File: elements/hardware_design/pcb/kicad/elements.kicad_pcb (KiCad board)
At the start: 2 copper layers, 164.5 x 106 mm, 198 parts, among them IC1 LM4040B10, IC10 STM32F405RGT6, IC11 4051PW, IC12 WM8731, IC13 MCP6004, IC14 LME49720, IC2 LM1117-3.3, IC3 4051PW, IC4 LM1117-3.3, IC5 4051PW, IC6 MCP6004, IC7 MCP6004, IC8 4051PW, IC9 MCP6002, J1 PJ301_THONKICONN6, J10 PJ301_THONKICONN6, J11 PJ301_THONKICONN6, J12 PJ301_THONKICONN6, J13 PJ301_THONKICONN6, J14 PJ301_THONKICONN6, J15 PJ301_THONKICONN6, J16 PJ301_THONKICONN6, J17 PJ301_THONKICONN6, J18 PJ301_THONKICONN6, J2 PJ301_THONKICONN6, J3 PJ301_THONKICONN6, J4 PJ301_THONKICONN6, J5 PJ301_THONKICONN6, J6 PJ301_THONKICONN6, J7 PJ301_THONKICONN6, J8 PJ301_THONKICONN6, J9 PJ301_THONKICONN6, Q1 8MHz, Q2 MMBT3904, SW1 LP4OA1PBCT

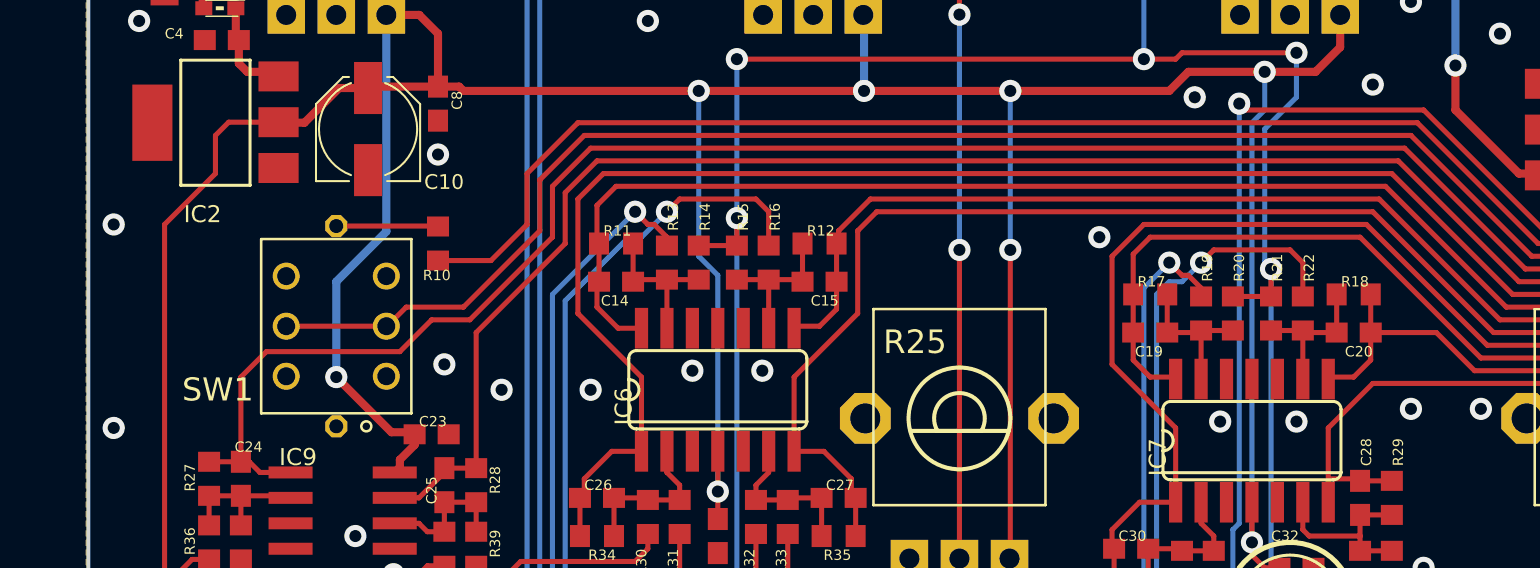
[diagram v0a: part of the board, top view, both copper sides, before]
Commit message: changed led/switch
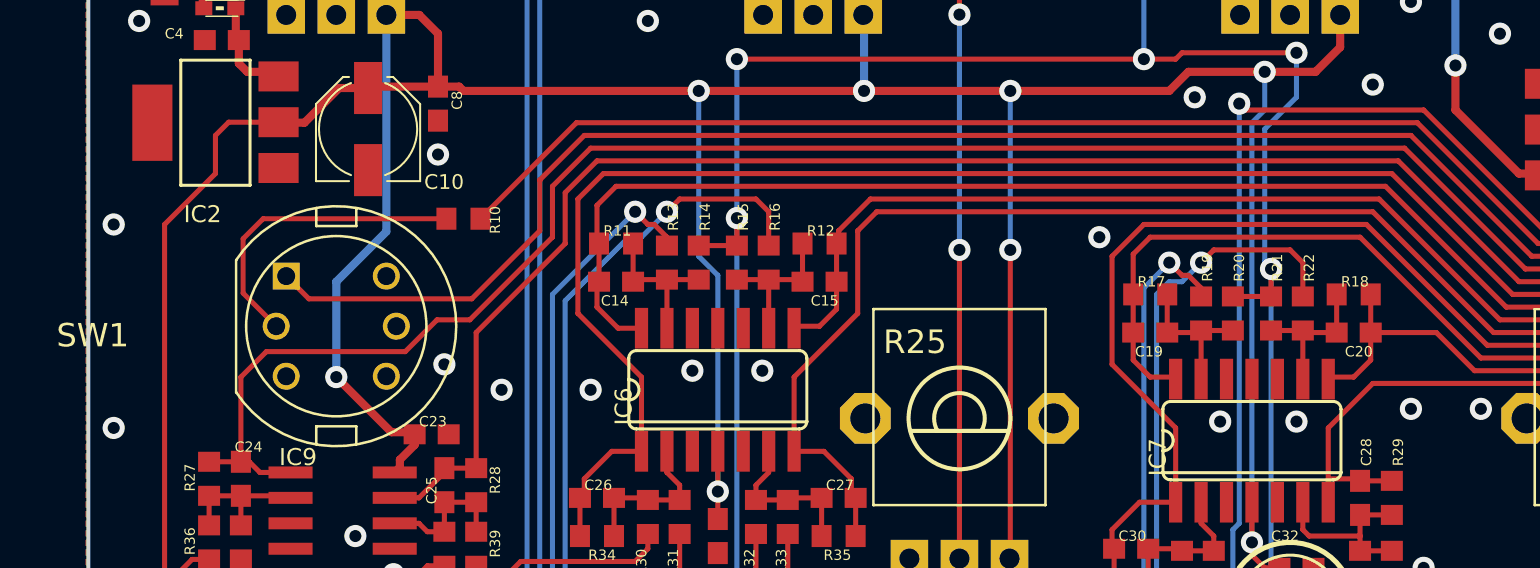
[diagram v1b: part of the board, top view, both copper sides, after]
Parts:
- removed U$2: , elements:ROHS_BIG
- JP2: value (none) -> M06SIP
- L1, L2: value (none) -> WE-CBF_0603
- SW1: value LP4OA1PBCT -> SW_MEC_5G_2LED; footprint elements:LP4OA1PBCT -> Supercell 1.3:C&K_D6R
- SW2, SW3: value (none) -> EVQQ2
- moved R10 1.77 mm to (85.0, 79.0), turned to 180 degrees
- turned SW1 to 0 degrees
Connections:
- net BOOT_FLASH renamed /elements_2/BOOT_FLASH
- net I2C_SCL renamed /elements_2/I2C_SCL
- net I2C_SDA renamed /elements_2/I2C_SDA
- net I2S_LRCK renamed /elements_2/I2S_LRCK
- net I2S_MCK renamed /elements_2/I2S_MCK
- net I2S_SCK renamed /elements_2/I2S_SCK
- net I2S_SIN renamed /elements_2/I2S_SIN
- net I2S_SOUT renamed /elements_2/I2S_SOUT
- net JTCK renamed /elements_2/JTCK
- net JTDI renamed /elements_2/JTDI
- net JTDO renamed /elements_2/JTDO
- net JTMS renamed /elements_2/JTMS
- net LOUT_JACK renamed Net-(J8-PadP3)
- net RESET renamed /elements_2/RESET
- net ROUT_JACK renamed Net-(J7-PadP3)
- net RX renamed /elements_2/RX
- net TX renamed /elements_2/TX
- IC10 pad 39: (no net) -> unconnected-(IC10-Pad39)
- IC10 pad 40: (no net) -> unconnected-(IC10-Pad40)
- IC10 pad 45: (no net) -> unconnected-(IC10-Pad45)
- IC10 pad 51: (no net) -> unconnected-(IC10-Pad51)
- IC10 pad 52: (no net) -> unconnected-(IC10-Pad52)
- IC10 pad 53: (no net) -> unconnected-(IC10-Pad53)
- IC10 pad 54: (no net) -> unconnected-(IC10-Pad54)
- IC10 pad 56: (no net) -> unconnected-(IC10-Pad56)
- IC10 pad 62: (no net) -> unconnected-(IC10-Pad62)
- IC12 pad 10: (no net) -> unconnected-(IC12-Pad10)
- IC12 pad 17: (no net) -> unconnected-(IC12-Pad17)
- IC12 pad 18: (no net) -> unconnected-(IC12-Pad18)
- IC12 pad 2: (no net) -> unconnected-(IC12-Pad2)
- IC12 pad 26: (no net) -> unconnected-(IC12-Pad26)
- IC12 pad 9: (no net) -> unconnected-(IC12-Pad9)
- J1 pad P2: (no net) -> unconnected-(J1-PadP2)
- J10 pad P2: (no net) -> unconnected-(J10-PadP2)
- J11 pad P2: (no net) -> unconnected-(J11-PadP2)
- J12 pad P2: (no net) -> unconnected-(J12-PadP2)
- J13 pad P2: (no net) -> unconnected-(J13-PadP2)
- J14 pad P2: (no net) -> unconnected-(J14-PadP2)
- J15 pad P2: (no net) -> unconnected-(J15-PadP2)
- J16 pad P2: (no net) -> unconnected-(J16-PadP2)
- J17 pad P2: (no net) -> unconnected-(J17-PadP2)
- J18 pad P2: (no net) -> unconnected-(J18-PadP2)
- J2 pad P2: (no net) -> unconnected-(J2-PadP2)
- J4 pad P2: (no net) -> unconnected-(J4-PadP2)
- J5 pad P2: (no net) -> unconnected-(J5-PadP2)
- J6 pad P2: (no net) -> unconnected-(J6-PadP2)
- J7 pad P2: (no net) -> unconnected-(J7-PadP2)
- J8 pad P2: (no net) -> unconnected-(J8-PadP2)
- J9 pad P2: (no net) -> unconnected-(J9-PadP2)
- JP1 pad 7: (no net) -> unconnected-(JP1-Pad7)
- JP2 pad 2: (no net) -> unconnected-(JP2-Pad2)
- JP2 pad 3: (no net) -> unconnected-(JP2-Pad3)
- JP2 pad 6: (no net) -> unconnected-(JP2-Pad6)
- R10 pad 2: N$38 -> Net-(R10-Pad2)
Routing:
- net Net-(R10-Pad2): track 0.00 -> 15.6 mm
- net N$38: track 5.09 -> 0.00 mm
- net LED_GATE: track 107.7 -> 103.3 mm

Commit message: change LME49720 to tl072
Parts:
- IC14: value LME49720 -> TL072
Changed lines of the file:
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@@
       (effects (font (size 0.84836 0.84836) (thickness 0.16764)) (justify left))
     )
-    (fp_text value "LME49720" (at -2.2225 1.0795) (layer "F.Fab")
+    (fp_text value "TL072" (at -2.2225 1.0795) (layer "F.Fab")
       (effects (font (size 0.44196 0.44196) (thickness 0.16764)) (justify left))
     )

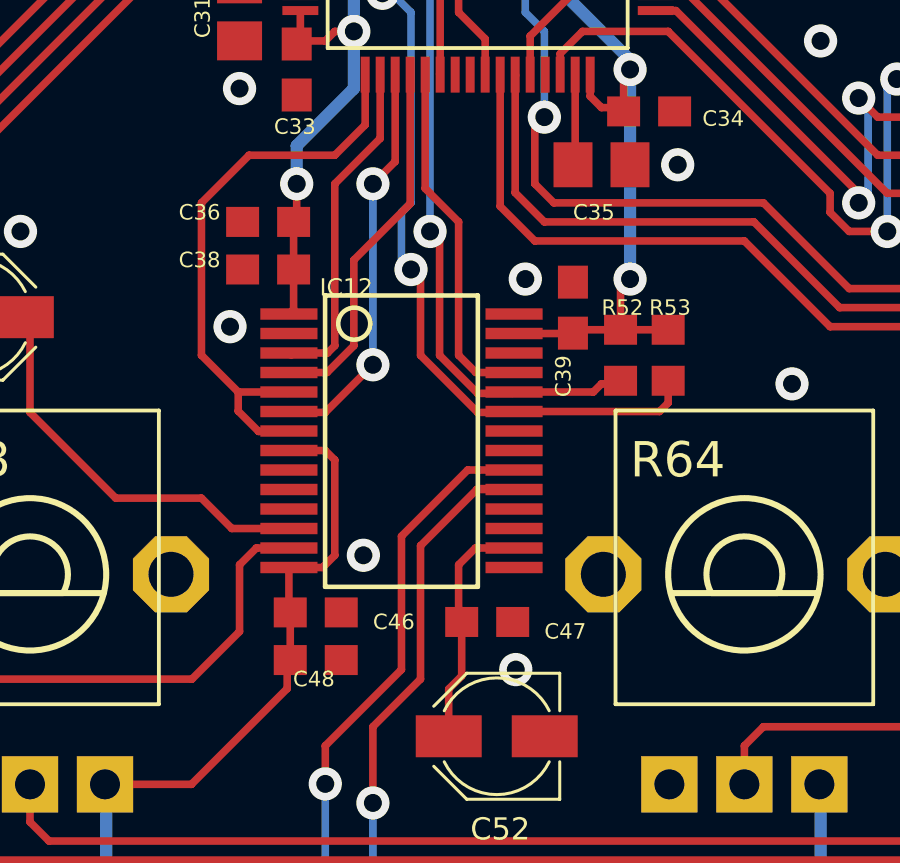
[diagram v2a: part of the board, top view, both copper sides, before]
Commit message: swap wm8731 package (haven't drawn traces yet)
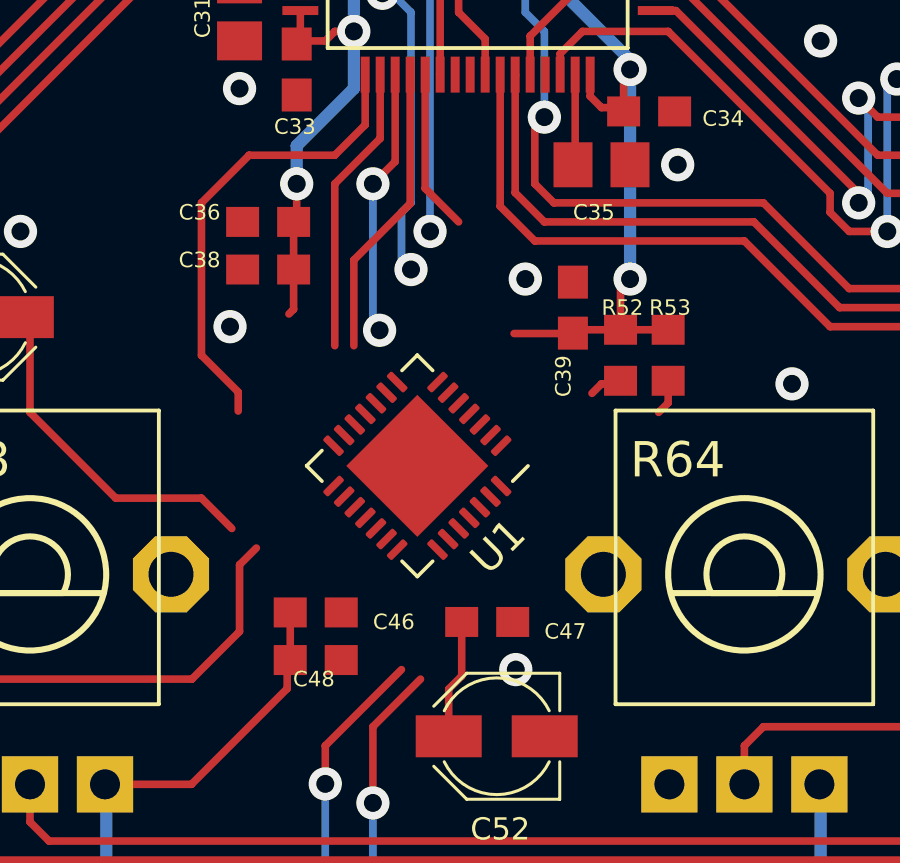
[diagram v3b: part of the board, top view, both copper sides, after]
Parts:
- removed IC12: WM8731, elements:SSOP28
- added U1: WM8731CLSEFL, Package_DFN_QFN:QFN-28-1EP_5x5mm_P0.5mm_EP3.35x3.35mm, F.Cu at (163.0, 112.5)
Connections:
- R52 pad 1: /elements_2/I2C_SCL -> /elements_2/I2C_SDA
- R53 pad 1: /elements_2/I2C_SDA -> /elements_2/I2C_SCL
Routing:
- net /elements_2/I2C_SDA: track 25.9 -> 14.5 mm
- net RIN: track 94.1 -> 84.5 mm
- net /elements_2/I2C_SCL: track 24.1 -> 14.8 mm
- net LIN: track 94.1 -> 85.0 mm
- net +3V3_A: track 885.1 -> 877.1 mm
- net /elements_2/I2S_MCK: track 11.9 -> 5.37 mm
- net /elements_2/I2S_SIN: track 13.4 -> 8.92 mm
- net Net-(U1-Pad20): track 8.02 -> 4.13 mm
- net /elements_2/I2S_LRCK: track 19.4 -> 15.7 mm
- net /elements_2/I2S_SOUT: track 12.3 -> 9.81 mm
- net LOUT: track 13.5 -> 11.6 mm
- net /elements_2/I2S_SCK: track 11.4 -> 9.66 mm
- net ROUT: track 20.1 -> 19.1 mm
- net GND: vias 146 -> 145

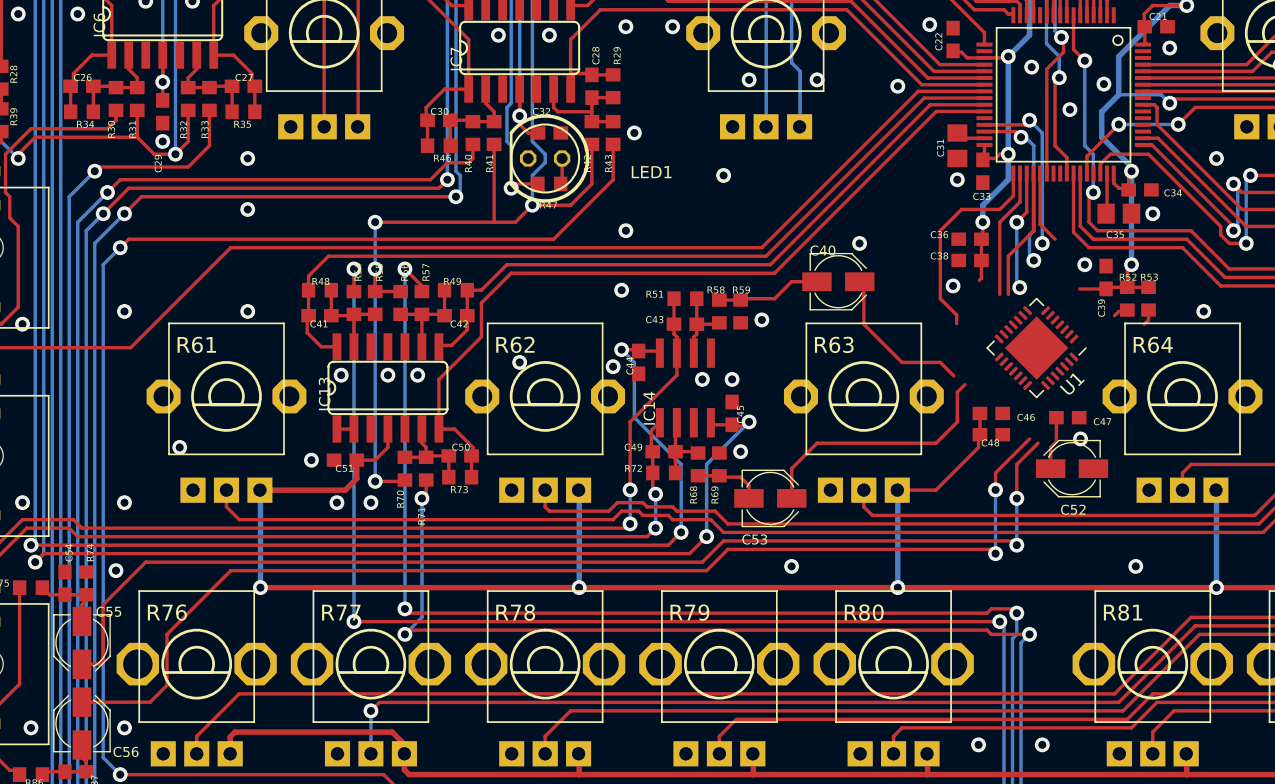
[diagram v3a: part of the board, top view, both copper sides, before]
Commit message: traces drawn for wm8731
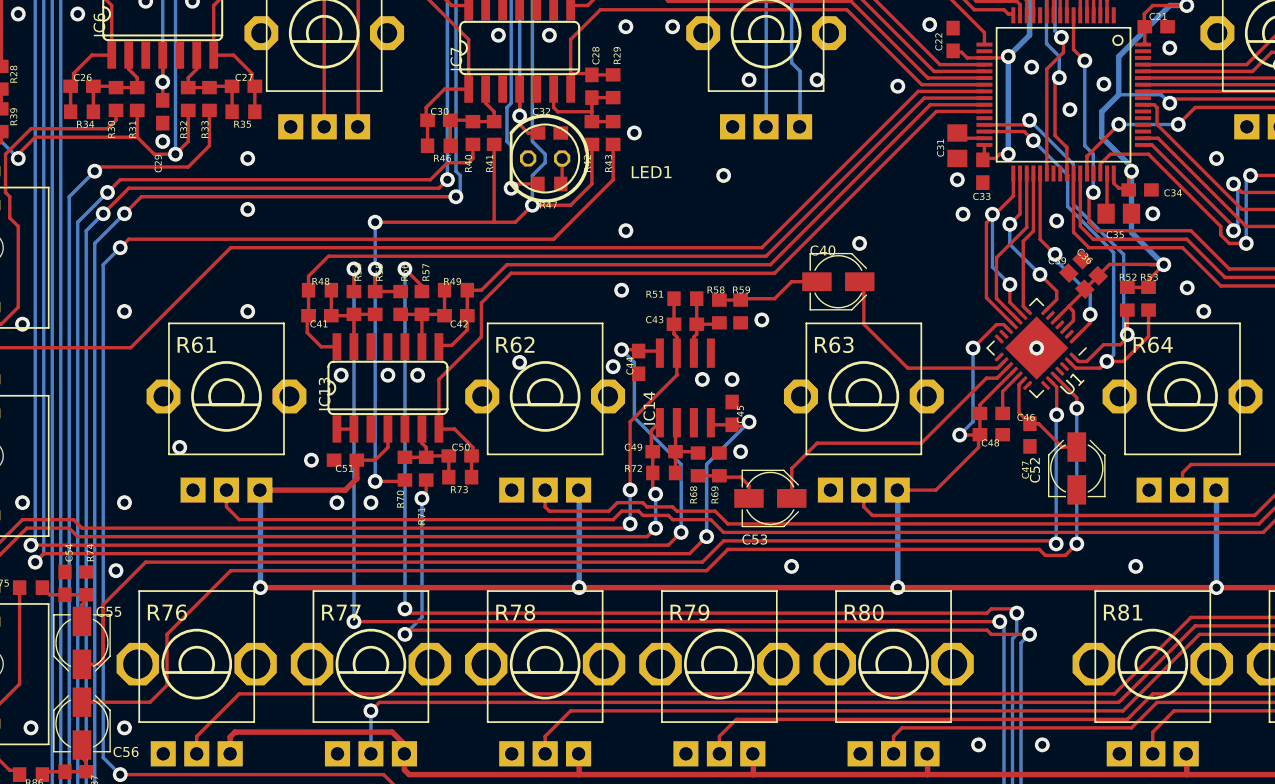
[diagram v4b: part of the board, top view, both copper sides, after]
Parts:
- removed C38: 100n, elements:C0603
- moved C36 9.22 mm to (167.0, 106.5), turned to 135 degrees
- moved C47 3.11 mm to (162.5, 119.0), turned to -90 degrees
- moved C39 2.20 mm to (166.0, 107.5), turned to 135 degrees
- moved C52 0.35 mm to (166.0, 121.5), turned to 90 degrees
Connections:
- R52 pad 1: /elements_2/I2C_SDA -> /elements_2/I2C_SCL
- R53 pad 1: /elements_2/I2C_SCL -> /elements_2/I2C_SDA
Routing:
- net /elements_2/I2C_SDA: track 14.5 -> 32.2 mm
- net +3V3_A: track 877.1 -> 893.3 mm, vias 25 -> 27
- net /elements_2/I2C_SCL: track 14.8 -> 29.5 mm
- net LIN: track 85.0 -> 95.1 mm
- net /elements_2/I2S_MCK: track 5.37 -> 14.4 mm, vias 0 -> 2
- net RIN: track 84.5 -> 91.5 mm
- net /elements_2/I2S_LRCK: track 15.7 -> 21.5 mm, vias 0 -> 2
- net Net-(C47-Pad1): track 4.13 -> 7.90 mm
- net LOUT: track 11.6 -> 15.3 mm
- net /elements_2/I2S_SIN: track 8.92 -> 12.6 mm, vias 2 -> 0
- net GND: track 0.04 -> 3.32 mm, vias 145 -> 146
- net /elements_2/I2S_SCK: track 9.66 -> 12.4 mm, vias 0 -> 2
- net ROUT: track 19.1 -> 21.6 mm
- net /elements_2/I2S_SOUT: track 9.81 -> 10.7 mm
- net +3V3: track 217.5 -> 218.0 mm, vias 12 -> 11

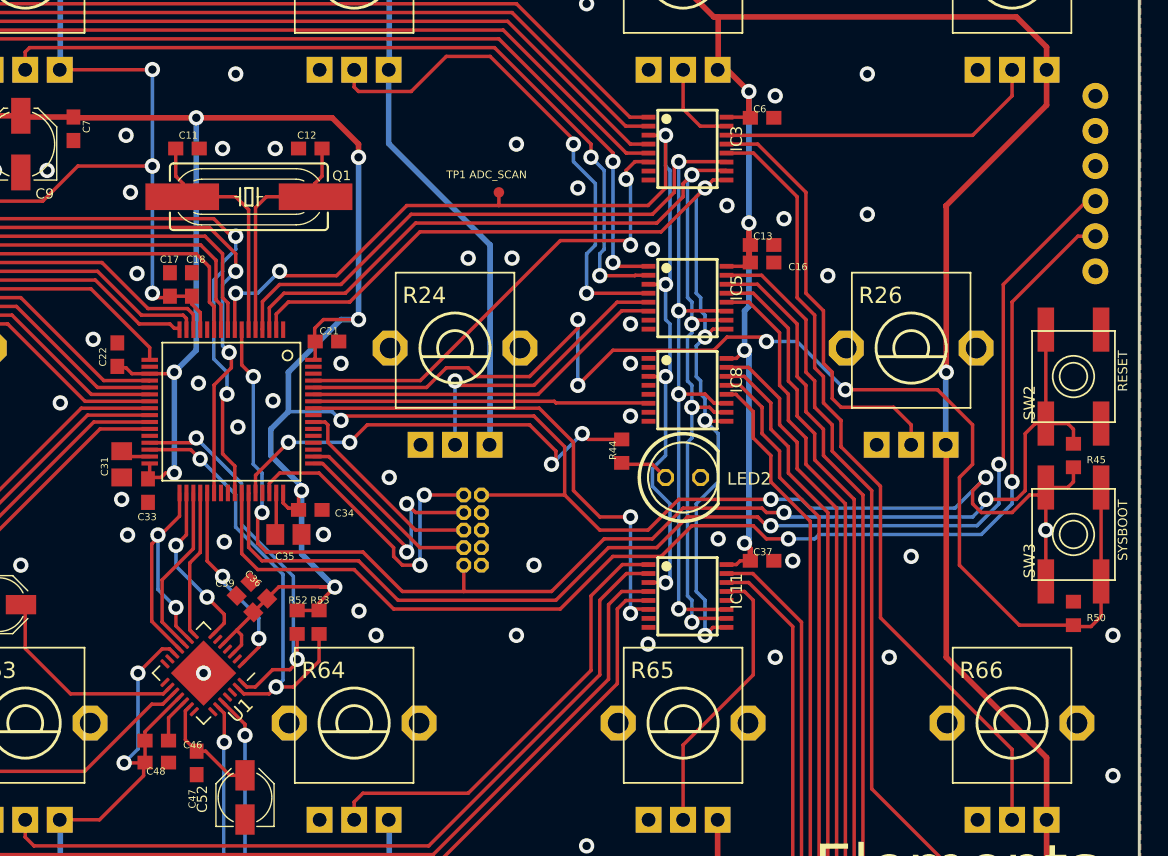
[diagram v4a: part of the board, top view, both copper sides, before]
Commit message: smaller boot/reset buttons
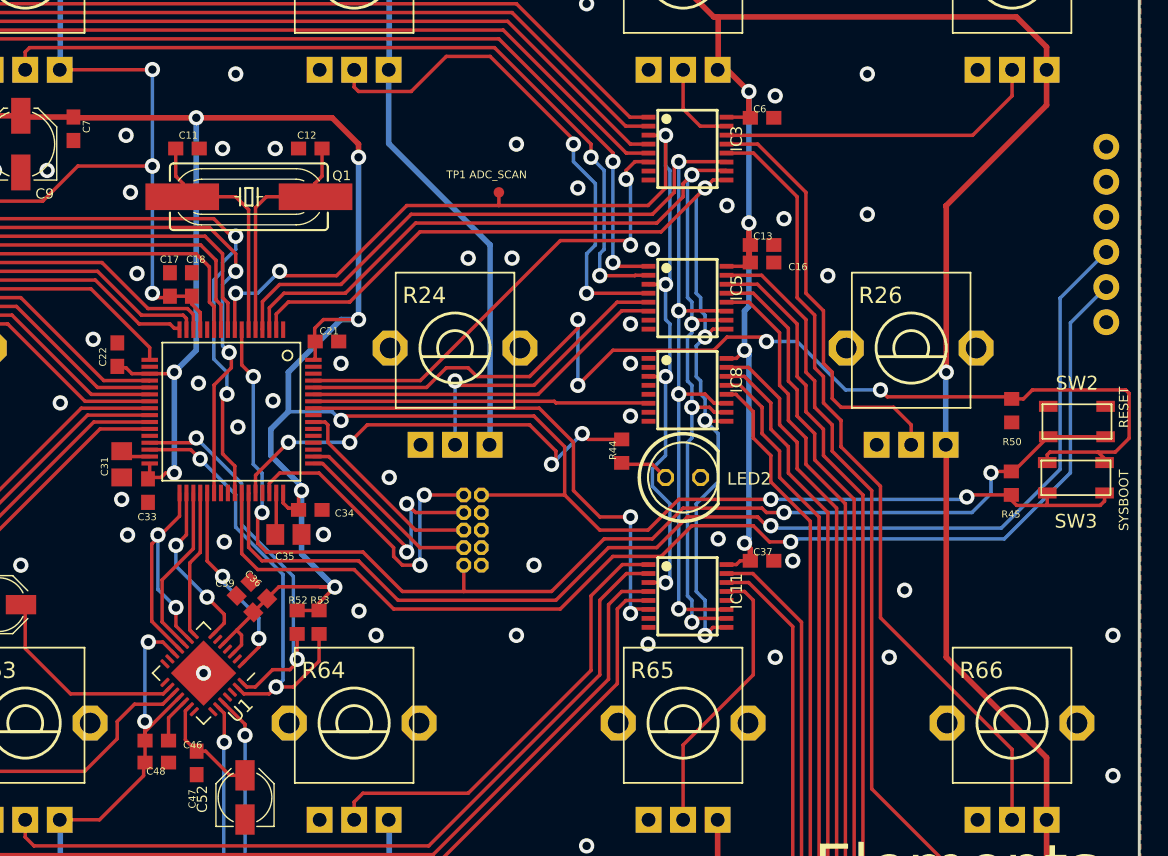
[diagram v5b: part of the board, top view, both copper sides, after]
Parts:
- SW2, SW3: footprint elements:EVQ-Q2 -> Supercell 1.3:k2-1808 pushbutton switch
- moved R50 15.3 mm to (221.5, 93.5), turned to 90 degrees
- moved R45 4.92 mm to (221.5, 98.8)
- moved SW3 4.11 mm to (226.1, 98.4), turned to 180 degrees
- moved JP2 3.76 mm to (228.3, 74.4)
- moved SW2 3.26 mm to (226.2, 94.3), turned to 180 degrees
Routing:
- net /elements_2/BOOT_FLASH: track 91.9 -> 81.7 mm
- net +3V3: track 218.0 -> 209.1 mm, vias 11 -> 10
- net /elements_2/RESET: track 94.8 -> 86.7 mm
- net /elements_2/TX: track 88.4 -> 85.6 mm, vias 2 -> 1
- net /elements_2/RX: track 88.5 -> 86.0 mm, vias 2 -> 1
- net +3V3_A: track 893.3 -> 890.8 mm
- net ROUT: track 21.6 -> 22.3 mm
